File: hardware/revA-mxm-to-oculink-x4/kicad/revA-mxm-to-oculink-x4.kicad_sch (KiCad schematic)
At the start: 0 parts

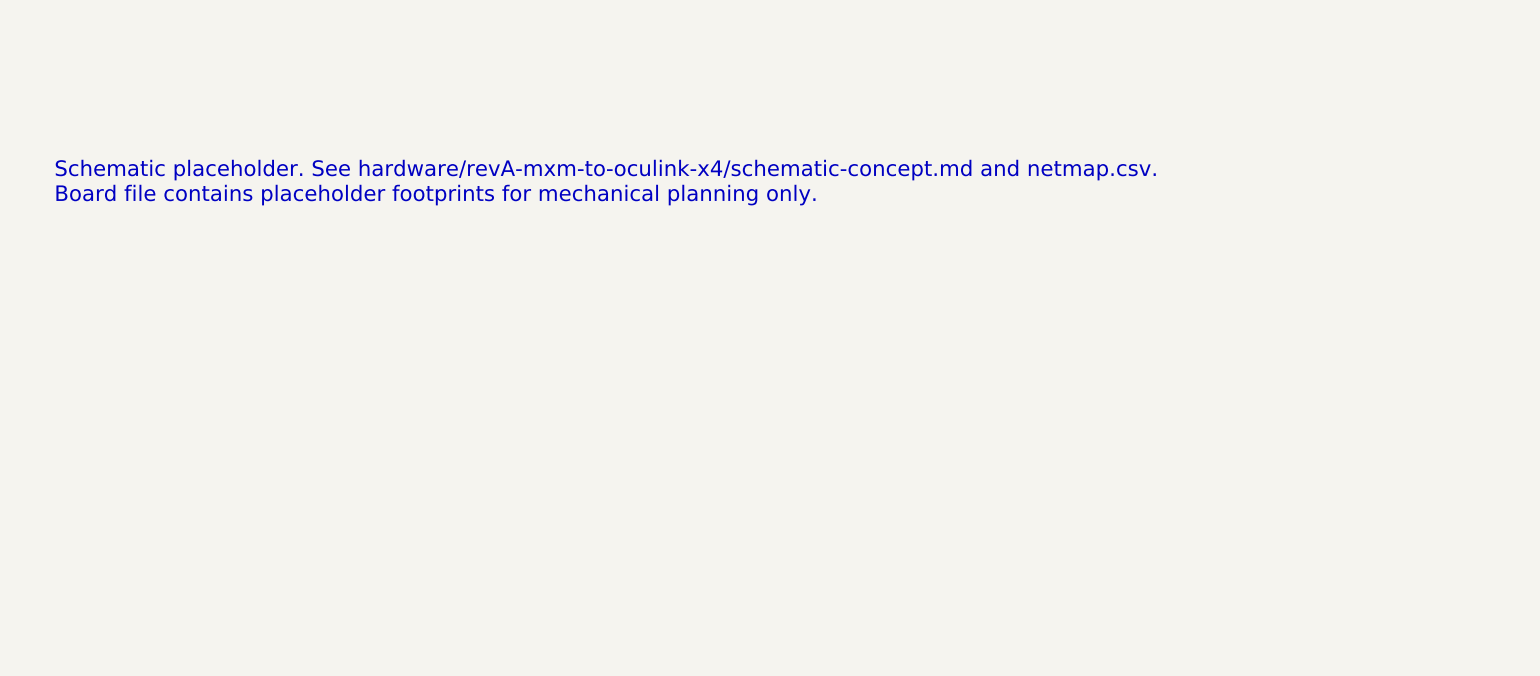
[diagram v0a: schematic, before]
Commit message: Expand KiCad schematic documentation stub
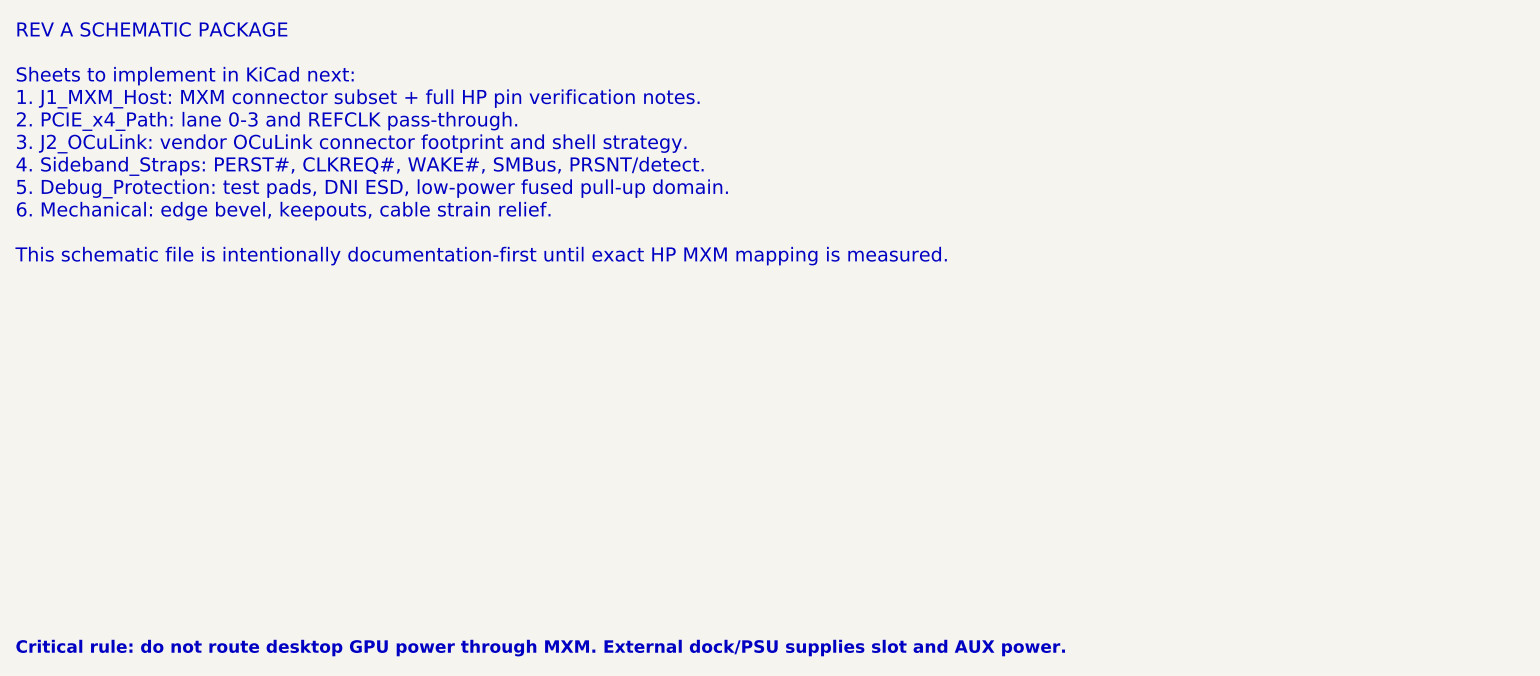
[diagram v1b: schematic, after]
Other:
- note added: "Critical rule: do not route desktop GPU power through MXM. External dock/PSU supplies slot and AUX power."
- note added: "REV A SCHEMATIC PACKAGE Sheets to implement in KiCad next: 1. J1_MXM_Host: MXM connector subset + full HP pin verification notes. 2. PCIE_x4_Path: lane 0-3 and REFCLK pass-through. 3. J2_OCuLink: vendor OCuLink connector footprint and shell strategy. 4. Sideband_Straps: PERST#, CLKREQ#, WAKE#, SMBus, PRSNT/detect. 5. Debug_Protection: test pads, DNI ESD, low-power fused pull-up domain. 6. Mechani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"
- note removed: "Schematic placeholder. See hardware/revA-mxm-to-oculink-x4/schematic-concept.md and netmap.csv. Board file contains placeholder footprints for mechanical planning only."
- title: RevA MXM to OCuLink x4 schematic skeleton -> RevA MXM to OCuLink x4 schematic package
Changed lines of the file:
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@@
 (kicad_sch
   (version 20231120)
-  (generator "ChatGPT RevA schematic skeleton")
+  (generator "ChatGPT RevA schematic package")
   (paper "A4")
   (title_block
-    (title "RevA MXM to OCuLink x4 schematic skeleton")
+    (title "RevA MXM to OCuLink x4 schematic package")
     (company "DerMilchjieper")
-    (comment 1 "Concept only - not fabrication-ready")
-    (comment 2 "MXM pin mapping and OCuLink footprint must be verified")
+    (rev "A-concept")
+    (comment 1 "NOT FABRICATION READY")
+    (comment 2 "MXM pin mapping, OCuLink footprint and stackup must be verified")
+    (comment 3 "See mxm_adapter.kicad_sym, pin-verification-matrix.csv, full-layout-plan.md")
   )
-  (text "Schematic placeholder. See hardware/revA-mxm-to-oculink-x4/schematic-concept.md and netmap.csv.\nBoard file contains placeholder footprints for mechanical planning only."
-    (at 25 25 0)
-    (effects (font (size 2 2)) (justify left))
+  (text "REV A SCHEMATIC PACKAGE\n\nSheets to implement in KiCad next:\n1. J1_MXM_Host: MXM connector subset + full HP pin verification notes.\n2. PCIE_x4_Path: lane 0-3 and REFCLK pass-through.\n3. J2_OCuLink: vendor OCuLink connector footprint and shell strategy.\n4. Sideband_Straps: PERST#, CLKREQ#, WAKE#, SMBus, PRSNT/detect.\n5. Debug_Protection: test pads, DNI ESD, low-power fused pull-up domain.\n6. Mechanical: edge bevel, keepouts, cable strain relief.\n\nThis schematic file is intentionally documentation-first until exact HP MXM mapping is measured."
+    (at 20 20 0)
+    (effects (font (size 1.8 1.8)) (justify left))
+  )
+  (text "Critical rule: do not route desktop GPU power through MXM. External dock/PSU supplies slot and AUX power."
+    (at 20 85 0)
+    (effects (font (size 1.6 1.6) (bold yes)) (justify left))
   )
 )
